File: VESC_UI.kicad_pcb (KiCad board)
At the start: 4 copper layers, 50 x 50 mm, 61 parts, among them J1 Hall_SS441R, J2 Hall_SS441R, J3 Conn_01x07_Male, J4 Conn_01x09_Female, J5 Conn_01x05_Male, J6 Conn_01x04_Male, J8 Conn_01x02_Male, J9 Conn_01x02_Male, Q1 Mosfet IRLML2060TRPBF, Q2 Mosfet IRLML2060TRPBF, SW1 Vertical push button, SW2 Vertical push button, SW3 Vertical push button, SW4 Vertical push button, SW5 Push button, U2 STM32F401CEU6, U3 M95M04-DR

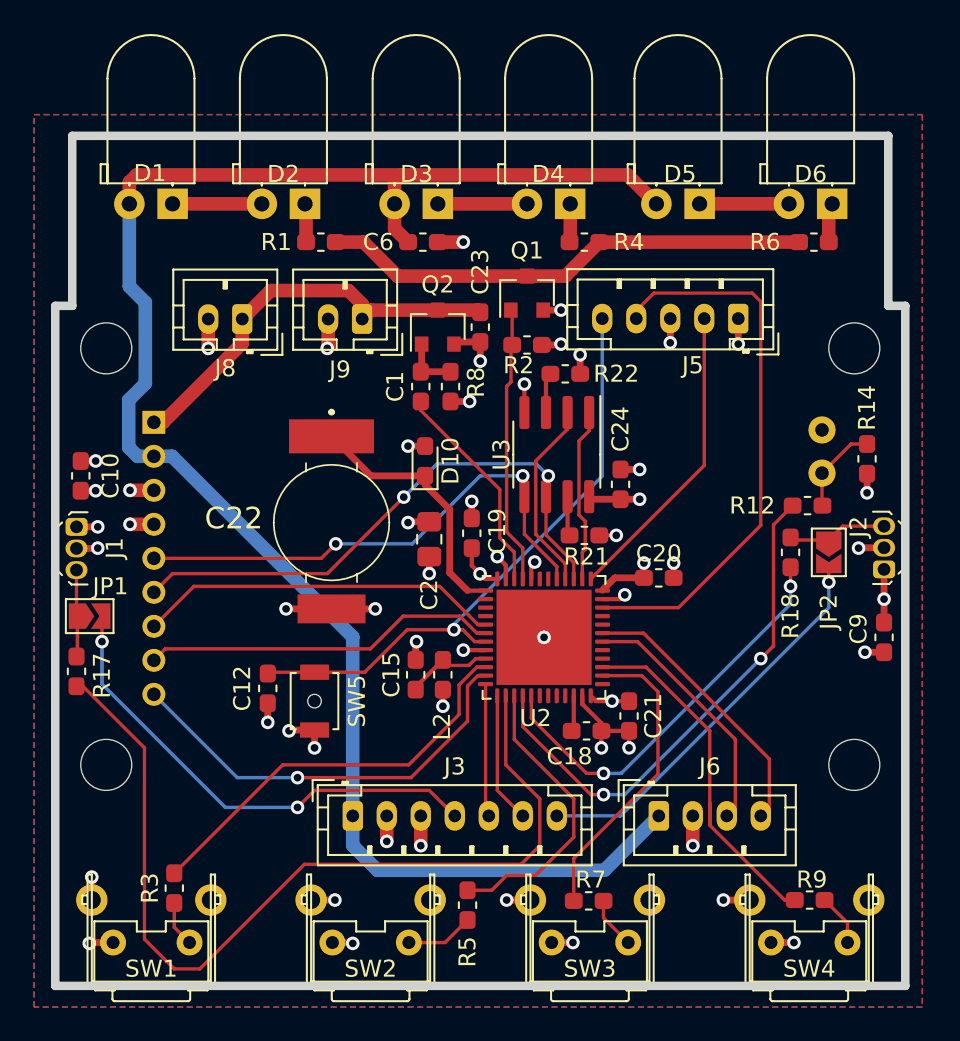
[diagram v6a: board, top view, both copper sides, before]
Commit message: Finalized PCBs
- Add MicroSD Card support on screen board
- Fix Hall sensors footprints (flip board side)
- Change screen connector
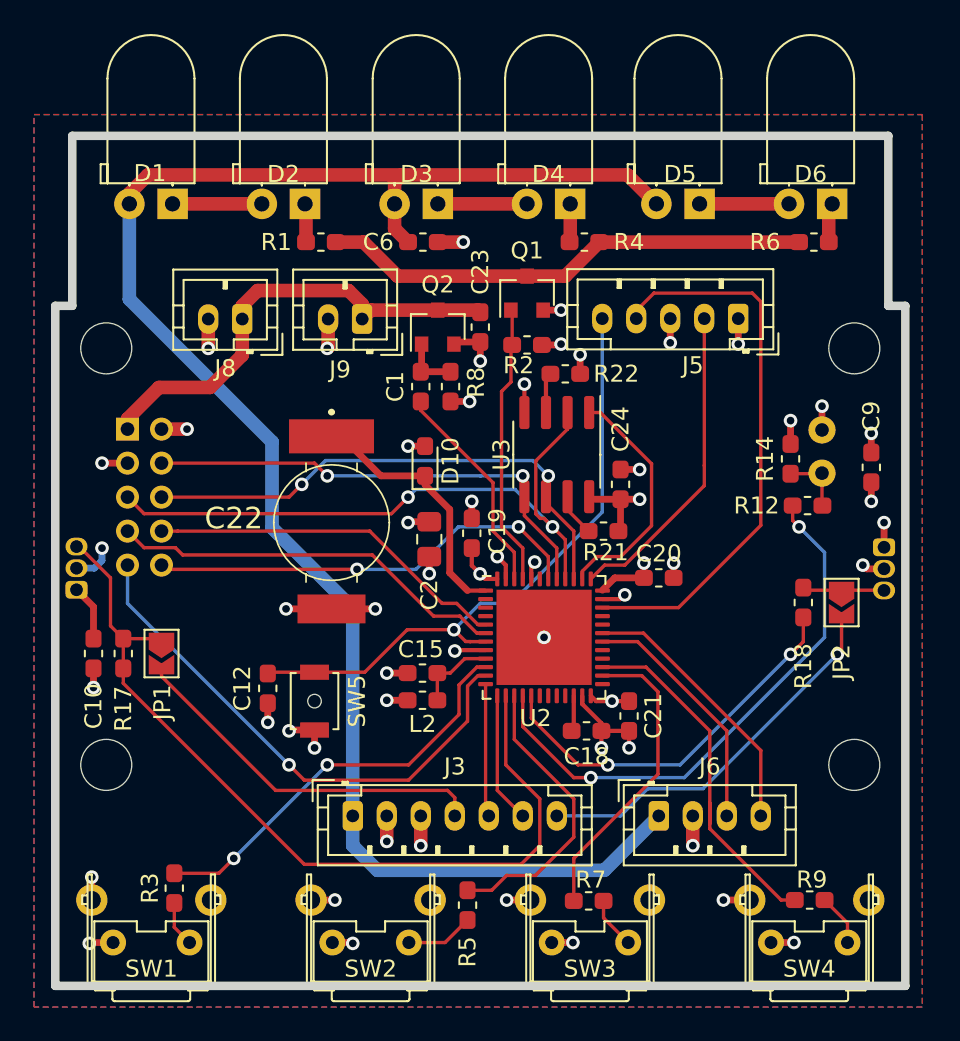
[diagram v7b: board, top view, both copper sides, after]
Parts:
- J1, J2: moved to B.Cu
- J4: value Conn_01x09_Female -> Conn_02x05_Female; footprint Connector_PinHeader_2.00mm:PinHeader_1x09_P2.00mm_Vertical -> Connector_PinSocket_2.00mm:PinSocket_2x05_P2.00mm_Vertical
- moved C10 10.5 mm to (116.2, 105.5), turned to 270 degrees
- moved C9 10.0 mm to (162.0, 94.5), turned to 90 degrees
- moved JP1 4.76 mm to (120.2, 105.5), turned to 270 degrees
- moved R14 4.50 mm to (157.2, 94.0), turned to 90 degrees
- moved J1 3.70 mm to (115.2, 101.7), turned to 90 degrees
- moved JP2 3.04 mm to (160.2, 102.5)
- moved R18 3.04 mm to (158.0, 102.5)
- moved R17 2.94 mm to (118.0, 105.5)
- moved L2 1.92 mm to (135.6, 108.2), turned to 0 degrees
- moved J4 1.60 mm to (118.2, 92.2)
- moved J2 1.30 mm to (162.8, 99.2), turned to 270 degrees
- moved R21 1.15 mm to (146.2, 98.2)
- moved C15 0.41 mm to (135.6, 106.6), turned to 180 degrees
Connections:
- J4 pad 2: +5V -> +3V3
- J4 pad 3: +3V3 -> GND
- J4 pad 4: GND -> /SPI1_MOSI
- J4 pad 5: /SPI1_MOSI -> /SPI1_MISO
- J4 pad 7: /OLED_CS -> /OLED_DC
- J4 pad 8: /OLED_DC -> /OLED_CS
- U2 pad 42: Net-(U2-Pad42) -> /SD_CS
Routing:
- net /SPI1_MISO: track 11.3 -> 38.3 mm, vias 0 -> 2
- net /SD_CS: track 0.00 -> 25.9 mm, vias 0 -> 2
- net /ADC1: track 53.4 -> 41.1 mm
- net /Accelerator: track 28.8 -> 21.9 mm, vias 2 -> 0
- net /OLED_RST: track 25.2 -> 31.4 mm
- net /EXT_FLASH_CS: track 10.3 -> 14.2 mm
- net Net-(J1-Pad3): track 5.13 -> 8.96 mm
- net +3V3: track 26.1 -> 29.4 mm, vias 15 -> 14
- net +12V: track 24.7 -> 27.7 mm
- net /SPI1_SCK: track 33.4 -> 30.8 mm
- net /OLED_DC: track 21.0 -> 23.5 mm
- net +5V: track 102.7 -> 100.3 mm
- net GND: track 61.6 -> 63.8 mm
- net /PHOTO_RESISTOR: track 30.6 -> 32.7 mm
- net /SPI1_MOSI: track 30.6 -> 28.5 mm
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
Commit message: fix(Mainboard): LEDs not working due to insufficient current
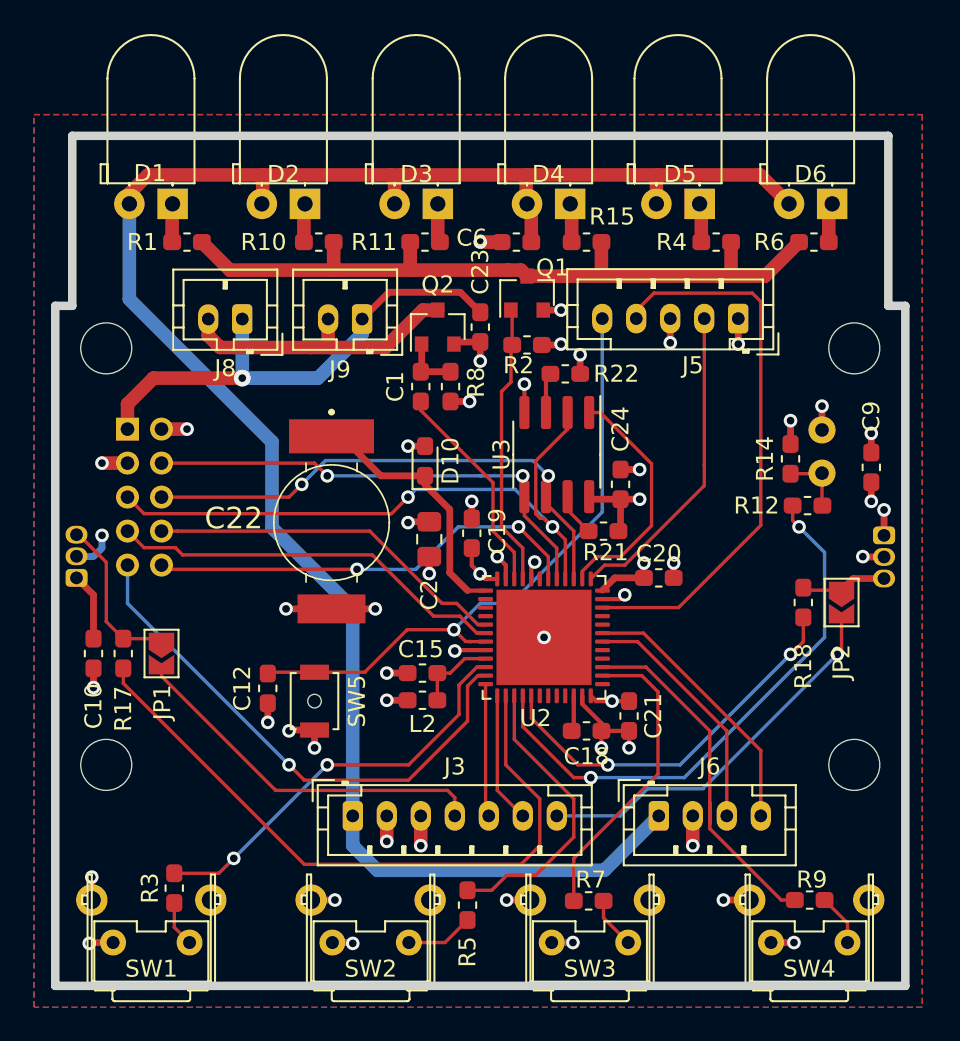
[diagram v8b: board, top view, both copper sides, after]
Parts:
- added R10: 62, Resistor_SMD:R_0603_1608Metric_Pad1.05x0.95mm_HandSolder, F.Cu at (129.5, 81.2)
- added R11: 62, Resistor_SMD:R_0603_1608Metric_Pad1.05x0.95mm_HandSolder, F.Cu at (135.8, 81.2)
- added R15: 62, Resistor_SMD:R_0603_1608Metric_Pad1.05x0.95mm_HandSolder, F.Cu at (145.2, 81.2)
- J1, J2: value Hall_SS441R -> Hall_DRV5055-Q1
- R1, R4, R6: value 30 -> 62
- moved R1 7.88 mm to (121.8, 81.2)
- moved R4 7.75 mm to (152.9, 81.2)
- moved C6 5.50 mm to (141.1, 81.2), turned to 0 degrees
- moved J1 0.70 mm to (115.2, 101.0)
- moved J2 0.70 mm to (162.8, 98.5)
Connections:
- D2 pad 2: Net-(D1-Pad1) -> +5V
- D4 pad 2: Net-(D3-Pad1) -> +5V
- D6 pad 2: Net-(D5-Pad1) -> +5V
- J8 pad 2: GND -> Net-(J8-Pad2)
- J9 pad 2: GND -> Net-(J8-Pad2)
- Q2 pad 3: +12V -> Net-(J8-Pad2)
- R1 pad 1: Net-(D2-Pad1) -> Net-(D1-Pad1)
- R4 pad 1: Net-(D4-Pad1) -> Net-(D5-Pad1)
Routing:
- net Net-(J8-Pad2): track 0.00 -> 17.9 mm
- net Net-(Q1-Pad3): track 28.9 -> 44.3 mm
- net +5V: track 100.3 -> 113.1 mm
- net GND: track 63.8 -> 60.0 mm, vias 42 -> 40
- net Net-(D1-Pad1): track 5.25 -> 2.26 mm
- net Net-(D5-Pad1): track 5.26 -> 2.29 mm
- net Net-(D3-Pad1): track 5.25 -> 2.30 mm
- net +12V: track 27.7 -> 29.4 mm, vias 0 -> 1
- net /ADC1: track 41.1 -> 39.9 mm
- net +3V3: track 29.4 -> 30.1 mm
- net Net-(J1-Pad3): track 8.96 -> 9.64 mm
